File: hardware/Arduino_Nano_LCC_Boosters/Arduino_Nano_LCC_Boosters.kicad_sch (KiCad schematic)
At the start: 11 parts, among them SW1 SW_Push, SW3 SW_Slide_DPDT, U1 DRV8874PWPR, U2 74HC04, U3 74HC00, U4 74HC86

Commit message: Board complete except power
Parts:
- removed C1: 22n, symbol Device:C
- removed C2: 100n, symbol Device:C
- removed C3: C100n, symbol Device:C
- removed R1: R, symbol Device:R
- removed U1: DRV8874PWPR, PWP0016J_N, symbol DRV8874:DRV8874PWPR
- removed U2: 74HC04, symbol 74xx:74HC04
- removed U3: 74HC00, symbol 74xx:74HC00
- removed U4: 74HC86, symbol 74xx:74HC86
- added J1: Screw_Terminal_01x12, symbol Connector:Screw_Terminal_01x12
- added J2: RJ45_LED_Shielded_x2, symbol Connector:RJ45_LED_Shielded_x2
- added R13, R14: R1k, symbol Device:R
- added R15: R10k, symbol Device:R
- added U11: MCP2515-xSO, Package_SO:SOIC-18W_7.5x11.6mm_P1.27mm, symbol Interface_CAN_LIN:MCP2515-xSO
- added U16: 7404, symbol 74xx_IEEE:7404
- added U19: MCP2551-I-SN, Package_SO:SOIC-8_3.9x4.9mm_P1.27mm, symbol Interface_CAN_LIN:MCP2551-I-SN
- added U6: ACPL-214-500E, Package_SO:SOP-4_4.4x2.6mm_P1.27mm, symbol Isolator:ACPL-214-500E
- added Y1: Crystal, symbol Device:Crystal
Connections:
- net brake_A is gone; now on net pwm_B: A1.12 (D9)
- net brake_D is gone; now on net pwm_C: A1.9 (D6)
- net scl is gone; now on net dir_B: A1.24 (A5)
- net sda is gone; now on net dir_A: A1.23 (A4)
- net +5V: now also R15.1, U11.18 (VDD), U19.3 (VDD)
- net GND: now also J1.2 (Pin_2), J2.15, J2.3, U11.9 (VSS), U16.7 (GND), U19.2 (VSS), U19.8 (Rs), U6.2
- net IOREF: now also R13.2, R14.2, U16.14 (VCC), U6.4
- net VTRACK: now also J1.1 (Pin_1)
- net dir_A: no longer A1.15 (D12)
- net dir_B: no longer A1.16 (D13)
- net dir_C: now also A1.5 (D2); no longer A1.13 (D10)
- net pwm_B: no longer A1.14 (D11)
- net pwm_C: no longer A1.5 (D2)
- net brake_B renamed led_2_n
- net led_2_n: now also J2.11
- net brake_C renamed led_1_n
- net led_1_n: now also J2.9
- new net: U11.1 (TXCAN), U19.1 (TXD)
- new net: R15.2, U11.17 (~{RESET})
- new net: U11.2 (RXCAN), U19.4 (RXD)
- new net: U11.7 (OSC2), Y1.1
- new net: U11.8 (OSC1), Y1.2
- new net: J2.12, R14.1
- new net: J2.10, R13.1
- new net Block Driver A/OUT1: J1.3 (Pin_3)
- new net Block Driver A/OUT2: J1.4 (Pin_4)
- new net Block Driver B/OUT1: J1.5 (Pin_5)
- new net Block Driver B/OUT2: J1.6 (Pin_6)
- new net Block Driver C/OUT1: J1.7 (Pin_7)
- new net Block Driver C/OUT2: J1.8 (Pin_8)
- new net Block Driver D/OUT1: J1.9 (Pin_9)
- new net Block Driver D/OUT2: J1.10 (Pin_10)
- new net can_h: J2.1, J2.13, U19.7 (CANH)
- new net can_l: J2.14, J2.2, U19.6 (CANL)
- new net can_shield: J2.18, J2.6, J2.SH, J2.SH
- new net cipo: A1.15 (D12), U11.15 (SO)
- new net copi: A1.14 (D11), U11.14 (SI)
- new net cs: A1.13 (D10), U11.16 (~{CS})
- new net dcc_n: J1.12 (Pin_12), U16.6
- new net dcc_p: J1.11 (Pin_11), U16.5, U6.3
- new net pwr_n: J2.19, J2.7
- new net pwr_p: J2.20, J2.8
- new net raw_dcc_n: J2.16, J2.4
- new net raw_dcc_p: J2.17, J2.5, U6.1
- new net sck: A1.16 (D13), U11.13 (SCK)
- no-connect marks 1 -> 13
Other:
- added sheet Block Driver A (block_driver.kicad_sch)
- added sheet Block Driver B (block_driver.kicad_sch)
- added sheet Block Driver C (block_driver.kicad_sch)
- added sheet Block Driver D (block_driver.kicad_sch)
- note removed: "Channel A"
- moved on the sheet: A1, SW1, SW3

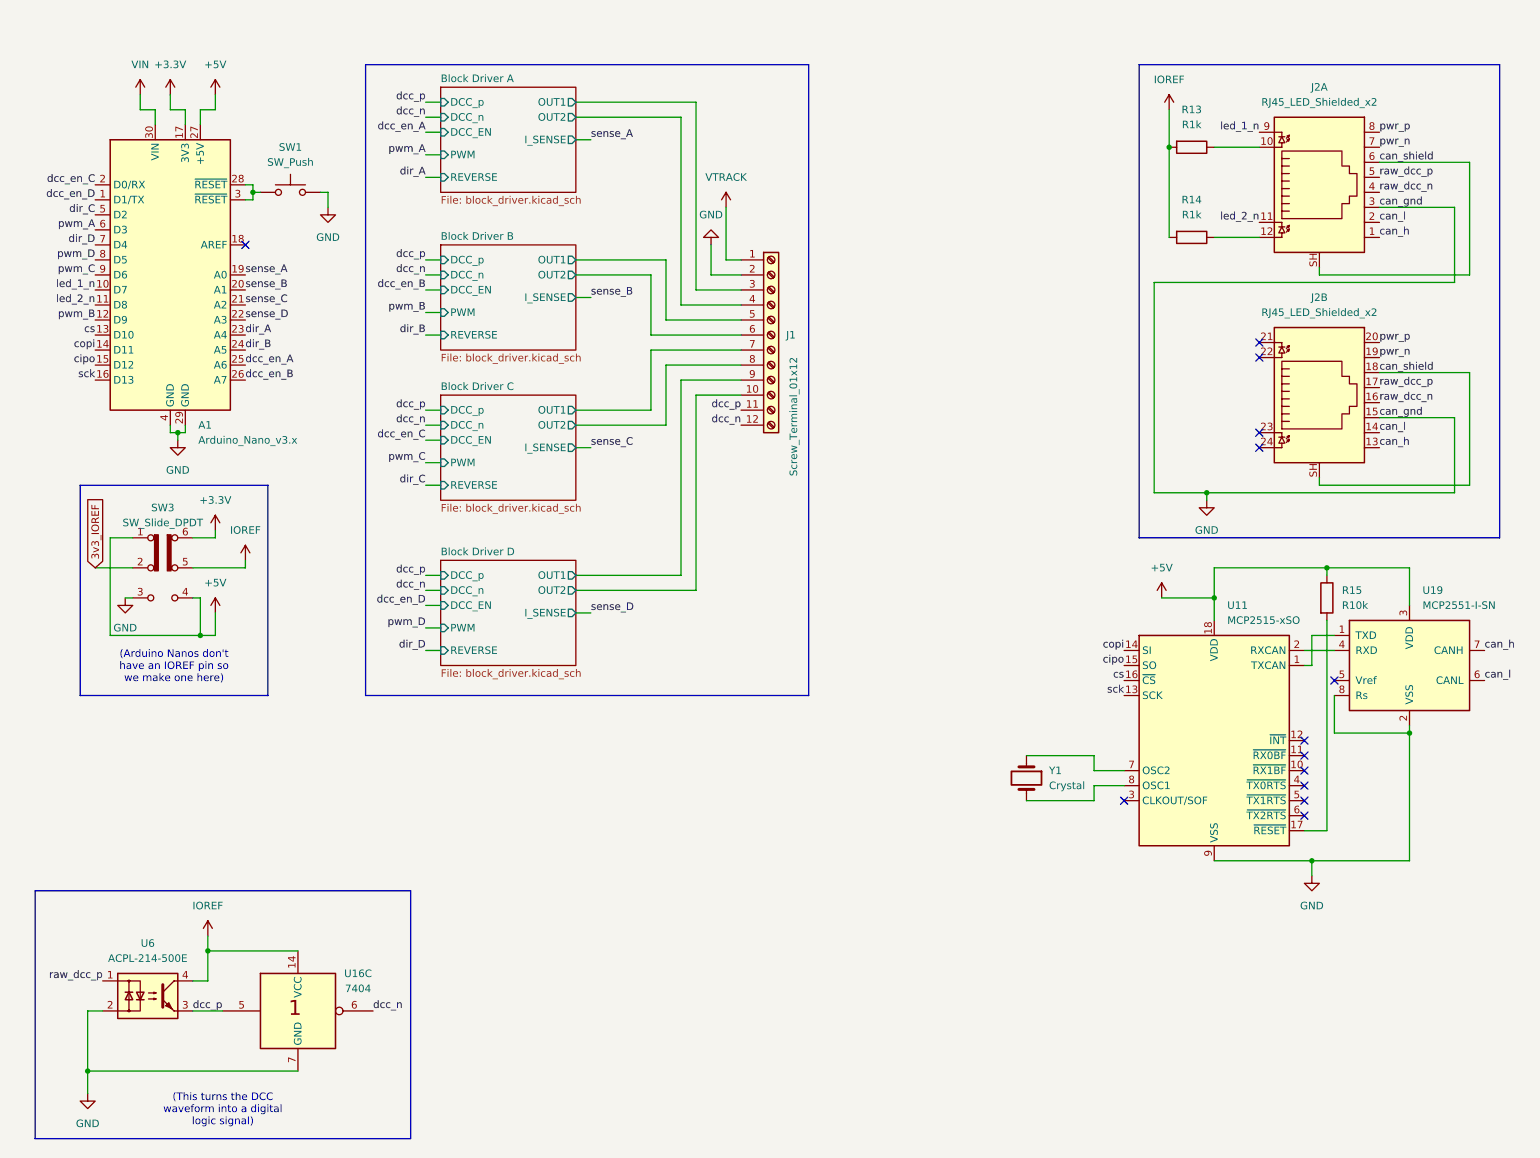
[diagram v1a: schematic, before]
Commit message: Made double nano board and updated CAN, added temporary power solution
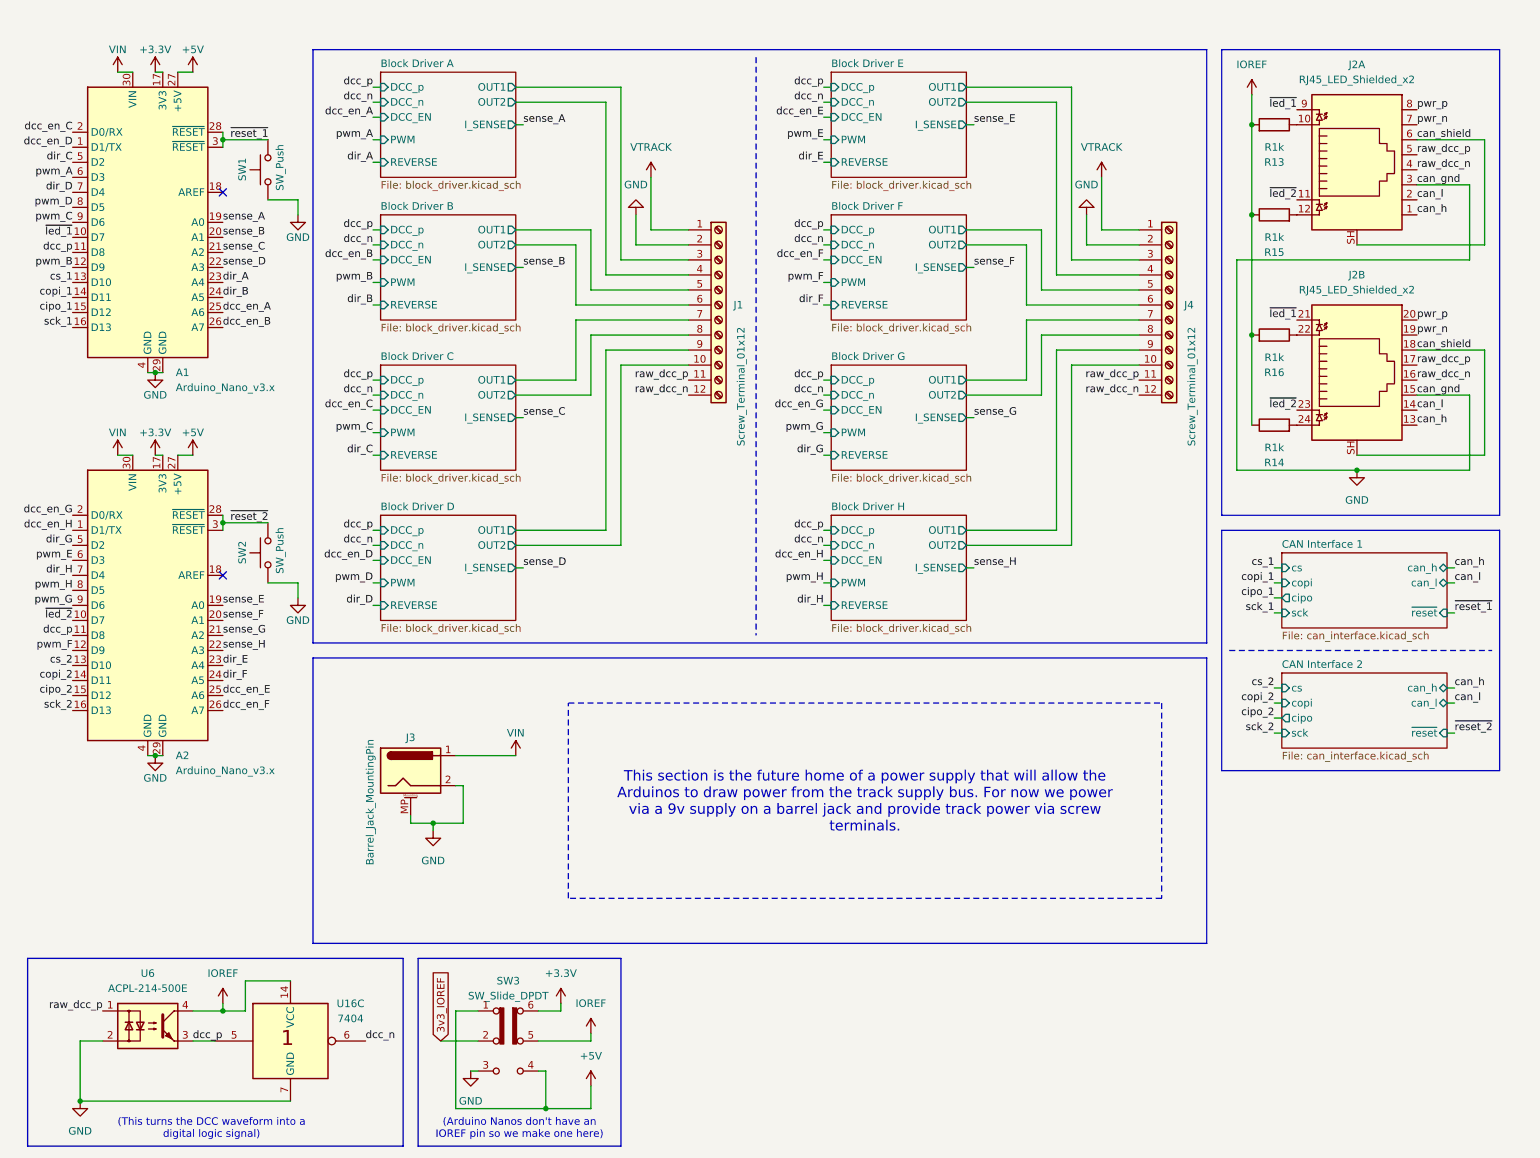
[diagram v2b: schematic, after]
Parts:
- removed U11: MCP2515-xSO, Package_SO:SOIC-18W_7.5x11.6mm_P1.27mm, symbol Interface_CAN_LIN:MCP2515-xSO
- removed U19: MCP2551-I-SN, Package_SO:SOIC-8_3.9x4.9mm_P1.27mm, symbol Interface_CAN_LIN:MCP2551-I-SN
- removed Y1: Crystal, symbol Device:Crystal
- added A2: Arduino_Nano_v3.x, Module:Arduino_Nano, symbol MCU_Module:Arduino_Nano_v3.x
- added J3: Barrel_Jack_MountingPin, symbol Connector:Barrel_Jack_MountingPin
- added J4: Screw_Terminal_01x12, symbol Connector:Screw_Terminal_01x12
- added R16: R1k, symbol Device:R
- added SW2: SW_Push, symbol Switch:SW_Push
- R15: value R10k -> R1k
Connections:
- net led_1_n is gone; now on net ~{led_1}: A1.10 (D7), J2.9
- net +3.3V: now also A2.17 (3V3)
- net +5V: now also A2.27 (+5V); no longer R15.1
- net GND: now also SW1.1, A2.29 (GND), A2.4 (GND), J3.2, J3.MP (MountPin), J4.2 (Pin_2), SW2.1; no longer SW1.2
- net IOREF: now also R14.1, R15.1, R16.2; no longer R14.2
- net VIN: now also A2.30 (VIN), J3.1
- net VTRACK: now also J4.1 (Pin_1)
- net dcc_n: no longer J1.12 (Pin_12)
- net dcc_p: now also A1.11 (D8), A2.11 (D8); no longer J1.11 (Pin_11)
- net raw_dcc_n: now also J1.12 (Pin_12), J4.12 (Pin_12)
- net raw_dcc_p: now also J1.11 (Pin_11), J4.11 (Pin_11)
- net at R15.2: now also J2.12
- net ~{reset_1}: now reaches A1.28 (~{RESET}), A1.3 (~{RESET})
- net ~{reset_1}: now also SW1.2; no longer SW1.1
- net ~{led_1}: now reaches J2.21
- net at J2.22: now also R16.1
- net ~{led_2}: now reaches J2.23
- net ~{led_2}: now also J2.11, A2.10 (D7)
- net at J2.24: now also R14.2
- net cipo renamed cipo_1
- net copi renamed copi_1
- net cs renamed cs_1
- removed net led_2_n: A1.11 (D8), J2.11
- net sck renamed sck_1
- new net Block Driver E/OUT1: J4.3 (Pin_3)
- new net Block Driver E/OUT2: J4.4 (Pin_4)
- new net Block Driver F/OUT1: J4.5 (Pin_5)
- new net Block Driver F/OUT2: J4.6 (Pin_6)
- new net Block Driver G/OUT1: J4.7 (Pin_7)
- new net Block Driver G/OUT2: J4.8 (Pin_8)
- new net Block Driver H/OUT1: J4.9 (Pin_9)
- new net Block Driver H/OUT2: J4.10 (Pin_10)
- new net cipo_2: A2.15 (D12)
- new net copi_2: A2.14 (D11)
- new net cs_2: A2.13 (D10)
- new net dcc_en_E: A2.25 (A6)
- new net dcc_en_F: A2.26 (A7)
- new net dcc_en_G: A2.2 (D0/RX)
- new net dcc_en_H: A2.1 (D1/TX)
- new net dir_E: A2.23 (A4)
- new net dir_F: A2.24 (A5)
- new net dir_G: A2.5 (D2)
- new net dir_H: A2.7 (D4)
- new net pwm_E: A2.6 (D3)
- new net pwm_F: A2.12 (D9)
- new net pwm_G: A2.9 (D6)
- new net pwm_H: A2.8 (D5)
- new net sck_2: A2.16 (D13)
- new net sense_E: A2.19 (A0)
- new net sense_F: A2.20 (A1)
- new net sense_G: A2.21 (A2)
- new net sense_H: A2.22 (A3)
- new net ~{reset_2}: A2.28 (~{RESET}), A2.3 (~{RESET}), SW2.2
- no-connect marks 13 -> 2
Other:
- added sheet Block Driver E (block_driver.kicad_sch)
- added sheet Block Driver F (block_driver.kicad_sch)
- added sheet Block Driver G (block_driver.kicad_sch)
- added sheet Block Driver H (block_driver.kicad_sch)
- added sheet CAN Interface 1 (can_interface.kicad_sch)
- added sheet CAN Interface 2 (can_interface.kicad_sch)
- moved on the sheet: A1, J1, J2A, J2B, R13, SW1, SW3, U16C, U6

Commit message: Started placement and routing
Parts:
- J1, J4: footprint (none) -> TerminalBlock_4Ucon:TerminalBlock_4Ucon_1x12_P3.50mm_Horizontal
- J2: footprint (none) -> Connector_RJ:RJ45_Amphenol_RJHSE538X-02
- J3: footprint (none) -> Connector_BarrelJack:BarrelJack_CUI_PJ-063AH_Horizontal
- R13, R14, R15, R16: footprint (none) -> Resistor_SMD:R_0815_2038Metric_Pad1.20x4.05mm_HandSolder
- SW1, SW2: footprint (none) -> Button_Switch_THT:SW_PUSH_6mm_H4.3mm
- SW3: footprint (none) -> Button_Switch_THT:SW_CK_JS202011CQN_DPDT_Straight
- U16: footprint (none) -> Package_SO:SO-14_5.3x10.2mm_P1.27mm
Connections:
- net Block Driver A/OUT1 renamed out1_A
- net Block Driver A/OUT2 renamed out2_A
- net Block Driver B/OUT1 renamed out1_B
- net Block Driver B/OUT2 renamed out2_B
- net Block Driver C/OUT1 renamed out1_C
- net Block Driver C/OUT2 renamed out2_C
- net Block Driver D/OUT1 renamed out1_D
- net Block Driver D/OUT2 renamed out2_D
- net Block Driver E/OUT1 renamed out1_E
- net Block Driver E/OUT2 renamed out2_E
- net Block Driver F/OUT1 renamed out1_F
- net Block Driver F/OUT2 renamed out2_F
- net Block Driver G/OUT1 renamed out1_G
- net Block Driver G/OUT2 renamed out2_G
- net Block Driver H/OUT1 renamed out1_H
- net Block Driver H/OUT2 renamed out2_H
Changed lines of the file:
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@@
 		)
 	)
+	(label "out2_B"
+		(at 99.06 48.26 0)
+		(fields_autoplaced yes)
+		(effects
+			(font
+				(size 1.27 1.27)
+			)
+			(justify left bottom)
+		)
+	)
 	(label "raw_dcc_p"
 		(at 250.19 33.02 0)
@@
 		)
 	)
+	(label "out1_G"
+		(at 175.26 71.12 0)
+		(fields_autoplaced yes)
+		(effects
+			(font
+				(size 1.27 1.27)
+			)
+			(justify left bottom)
+		)
+	)
 	(label "~{led_1}"
 		(at 229.87 25.4 180)
@@
 		)
 	)
+	(label "out2_F"
+		(at 175.26 48.26 0)
+		(fields_autoplaced yes)
+		(effects
+			(font
+				(size 1.27 1.27)
+			)
+			(justify left bottom)
+		)
+	)
 	(label "dcc_p"
 		(at 73.66 71.12 180)
@@
 		)
 	)
+	(label "out2_A"
+		(at 99.06 24.13 0)
+		(fields_autoplaced yes)
+		(effects
+			(font
+				(size 1.27 1.27)
+			)
+			(justify left bottom)
+		)
+	)
 	(label "sck_2"
 		(at 22.86 127 180)
@@
 		)
 	)
+	(label "out1_F"
+		(at 175.26 45.72 0)
+		(fields_autoplaced yes)
+		(effects
+			(font
+				(size 1.27 1.27)
+			)
+			(justify left bottom)
+		)
+	)
+	(label "out2_C"
+		(at 99.06 73.66 0)
+		(fields_autoplaced yes)
+		(effects
+			(font
+				(size 1.27 1.27)
+			)
+			(justify left bottom)
+		)
+	)
 	(label "dir_B"
 		(at 73.66 58.42 180)
@@
 		)
 	)
+	(label "out1_E"
+		(at 175.26 21.59 0)
+		(fields_autoplaced yes)
+		(effects
+			(font
+				(size 1.27 1.27)
+			)
+			(justify left bottom)
+		)
+	)
 	(label "dcc_en_A"
 		(at 48.26 59.69 0)
@@
 		)
 	)
+	(label "out1_D"
+		(at 99.06 96.52 0)
+		(fields_autoplaced yes)
+		(effects
+			(font
+				(size 1.27 1.27)
+			)
+			(justify left bottom)
+		)
+	)
 	(label "pwm_C"
 		(at 73.66 80.01 180)
@@
 		)
 	)
+	(label "out1_H"
+		(at 175.26 96.52 0)
+		(fields_autoplaced yes)
+		(effects
+			(font
+				(size 1.27 1.27)
+			)
+			(justify left bottom)
+		)
+	)
 	(label "cipo_1"
 		(at 22.86 59.69 180)
@@
 		)
 	)
+	(label "out2_D"
+		(at 99.06 99.06 0)
+		(fields_autoplaced yes)
+		(effects
+			(font
+				(size 1.27 1.27)
+			)
+			(justify left bottom)
+		)
+	)
 	(label "dcc_n"
 		(at 73.66 99.06 180)
@@
 		)
 	)
+	(label "out2_G"
+		(at 175.26 73.66 0)
+		(fields_autoplaced yes)
+		(effects
+			(font
+				(size 1.27 1.27)
+			)
+			(justify left bottom)
+		)
+	)
 	(label "can_shield"
 		(at 250.19 30.48 0)
@@
 		)
 	)
+	(label "out1_C"
+		(at 99.06 71.12 0)
+		(fields_autoplaced yes)
+		(effects
+			(font
+				(size 1.27 1.27)
+			)
+			(justify left bottom)
+		)
+	)
 	(label "sck_1"
 		(at 22.86 62.23 180)
@@
 		)
 	)
+	(label "out2_H"
+		(at 175.26 99.06 0)
+		(fields_autoplaced yes)
+		(effects
+			(font
+				(size 1.27 1.27)
+			)
+			(justify left bottom)
+		)
+	)
 	(label "dcc_en_A"
 		(at 73.66 26.67 180)
@@
 		)
 	)
+	(label "out1_A"
+		(at 99.06 21.59 0)
+		(fields_autoplaced yes)
+		(effects
+			(font
+				(size 1.27 1.27)
+			)
+			(justify left bottom)
+		)
+	)
 	(label "copi_1"
 		(at 226.06 105.41 180)
@@
 		)
 	)
+	(label "out2_E"
+		(at 175.26 24.13 0)
+		(fields_autoplaced yes)
+		(effects
+			(font
+				(size 1.27 1.27)
+			)
+			(justify left bottom)
+		)
+	)
 	(label "~{reset_2}"
 		(at 256.54 130.81 0)
@@
 		)
 	)
+	(label "out1_B"
+		(at 99.06 45.72 0)
+		(fields_autoplaced yes)
+		(effects
+			(font
+				(size 1.27 1.27)
+			)
+			(justify left bottom)
+		)
+	)
 	(label "dcc_en_H"
 		(at 22.86 96.52 180)
@@
 			)
 		)
-		(property "Footprint" ""
+		(property "Footprint" "TerminalBlock_4Ucon:TerminalBlock_4Ucon_1x12_P3.50mm_Horizontal"
 			(at 208.28 58.42 0)
 			(effects
@@
 		(on_board yes)
 		(dnp no)
-		(property "Reference" "#PWR01"
+		(property "Reference" "#PWR0102"
 			(at 30.48 22.86 0)
 			(effects
@@
 			(project "Arduino_Nano_LCC_Boosters"
 				(path "/fe98a12a-bd47-40d6-885d-b688d74230c5"
-					(reference "#PWR01")
+					(reference "#PWR0102")
 					(unit 1)
 				)
@@
 			)
 		)
-		(property "Footprint" ""
+		(property "Footprint" "Connector_BarrelJack:BarrelJack_CUI_PJ-063AH_Horizontal"
 			(at 81.28 138.176 0)
 			(effects
@@
 			)
 		)
-		(property "Footprint" ""
+		(property "Footprint" "Resistor_SMD:R_0815_2038Metric_Pad1.20x4.05mm_HandSolder"
 			(at 226.06 65.278 90)
 			(effects
@@
 			)
 		)
-		(property "Footprint" ""
+		(property "Footprint" "Package_SO:SO-14_5.3x10.2mm_P1.27mm"
 			(at 59.69 182.88 0)
 			(effects
@@
 		(on_board yes)
 		(dnp no)
-		(property "Reference" "#PWR02"
+		(property "Reference" "#PWR0101"
 			(at 43.18 22.86 0)
 			(effects
@@
 			(project "Arduino_Nano_LCC_Boosters"
 				(path "/fe98a12a-bd47-40d6-885d-b688d74230c5"
-					(reference "#PWR02")
+					(reference "#PWR0101")
 					(unit 1)
 				)
@@
 			)
 		)
-		(property "Footprint" ""
+		(property "Footprint" "Button_Switch_THT:SW_PUSH_6mm_H4.3mm"
 			(at 50.8 35.56 0)
 			(effects
@@
 			)
 		)
-		(property "Footprint" ""
+		(property "Footprint" "Button_Switch_THT:SW_CK_JS202011CQN_DPDT_Straight"
 			(at 110.49 177.8 0)
 			(effects
@@
 			)
 		)
-		(property "Footprint" ""
+		(property "Footprint" "TerminalBlock_4Ucon:TerminalBlock_4Ucon_1x12_P3.50mm_Horizontal"
 			(at 132.08 58.42 0)
 			(effects
@@
 			)
 		)
-		(property "Footprint" ""
+		(property "Footprint" "Connector_RJ:RJ45_Amphenol_RJHSE538X-02"
 			(at 240.03 34.925 90)
 			(effects
@@
 			)
 		)
-		(property "Footprint" ""
+		(property "Footprint" "Resistor_SMD:R_0815_2038Metric_Pad1.20x4.05mm_HandSolder"
 			(at 226.06 44.958 90)
 			(effects
@@
 			)
 		)
-		(property "Footprint" ""
+		(property "Footprint" "Connector_RJ:RJ45_Amphenol_RJHSE538X-02"
 			(at 240.03 70.485 90)
 			(effects
@@
 			)
 		)
-		(property "Footprint" ""
+		(property "Footprint" "Resistor_SMD:R_0815_2038Metric_Pad1.20x4.05mm_HandSolder"
 			(at 226.06 80.518 90)
 			(effects
@@
 			)
 		)
-		(property "Footprint" ""
+		(property "Footprint" "Resistor_SMD:R_0815_2038Metric_Pad1.20x4.05mm_HandSolder"
 			(at 226.06 29.718 90)
 			(effects
@@
 			)
 		)
-		(property "Footprint" ""
+		(property "Footprint" "Button_Switch_THT:SW_PUSH_6mm_H4.3mm"
 			(at 50.8 100.33 0)
 			(effects

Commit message: Switch to single Arduino per board
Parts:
- removed J1, J4: Screw_Terminal_01x12, TerminalBlock_4Ucon:TerminalBlock_4Ucon_1x12_P3.50mm_Horizontal, symbol Connector:Screw_Terminal_01x12
- removed U16: 7404, Package_SO:SO-14_5.3x10.2mm_P1.27mm, symbol 74xx_IEEE:7404
- added J2, J5: Screw_Terminal_01x08, TerminalBlock_Phoenix:TerminalBlock_Phoenix_MKDS-1,5-8_1x08_P5.00mm_Horizontal, symbol Connector:Screw_Terminal_01x08
- added J3, J4: Screw_Terminal_01x02, TerminalBlock_Phoenix:TerminalBlock_Phoenix_MKDS-1,5-2_1x02_P5.00mm_Horizontal, symbol Connector:Screw_Terminal_01x02
- renumbered J3 to J1, J2 to J6, R13 to R1, R15 to R2, R16 to R3, R14 to R4, U6 to U1
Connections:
- net GND: now also J3.2 (Pin_2)
- net VTRACK: now also J3.1 (Pin_1)
- net out1_A: now also J2.1 (Pin_1)
- net out1_B: now also J2.3 (Pin_3)
- net out1_C: now also J2.5 (Pin_5)
- net out1_D: now also J2.7 (Pin_7)
- net out1_E: now also J5.1 (Pin_1)
- net out1_F: now also J5.3 (Pin_3)
- net out1_G: now also J5.5 (Pin_5)
- net out1_H: now also J5.7 (Pin_7)
- net out2_A: now also J2.2 (Pin_2)
- net out2_B: now also J2.4 (Pin_4)
- net out2_C: now also J2.6 (Pin_6)
- net out2_D: now also J2.8 (Pin_8)
- net out2_E: now also J5.2 (Pin_2)
- net out2_F: now also J5.4 (Pin_4)
- net out2_G: now also J5.6 (Pin_6)
- net out2_H: now also J5.8 (Pin_8)
- net raw_dcc_n: now also J4.2 (Pin_2)
- net raw_dcc_p: now also J4.1 (Pin_1)
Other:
- sheet Block Driver A ports: added none; removed DCC_n
- sheet Block Driver B ports: added none; removed DCC_n
- sheet Block Driver C ports: added none; removed DCC_n
- sheet Block Driver D ports: added none; removed DCC_n
- sheet Block Driver E ports: added none; removed DCC_n
- sheet Block Driver F ports: added none; removed DCC_n
- sheet Block Driver G ports: added none; removed DCC_n
- sheet Block Driver H ports: added none; removed DCC_n
- moved on the sheet: U1
